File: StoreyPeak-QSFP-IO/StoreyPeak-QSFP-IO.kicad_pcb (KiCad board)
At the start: 2 copper layers, 30.1 x 69.8 mm, 29 parts, among them U1 QSFP_PCB-QSFP, U3 CH340G, X1 X322512MSB4SI

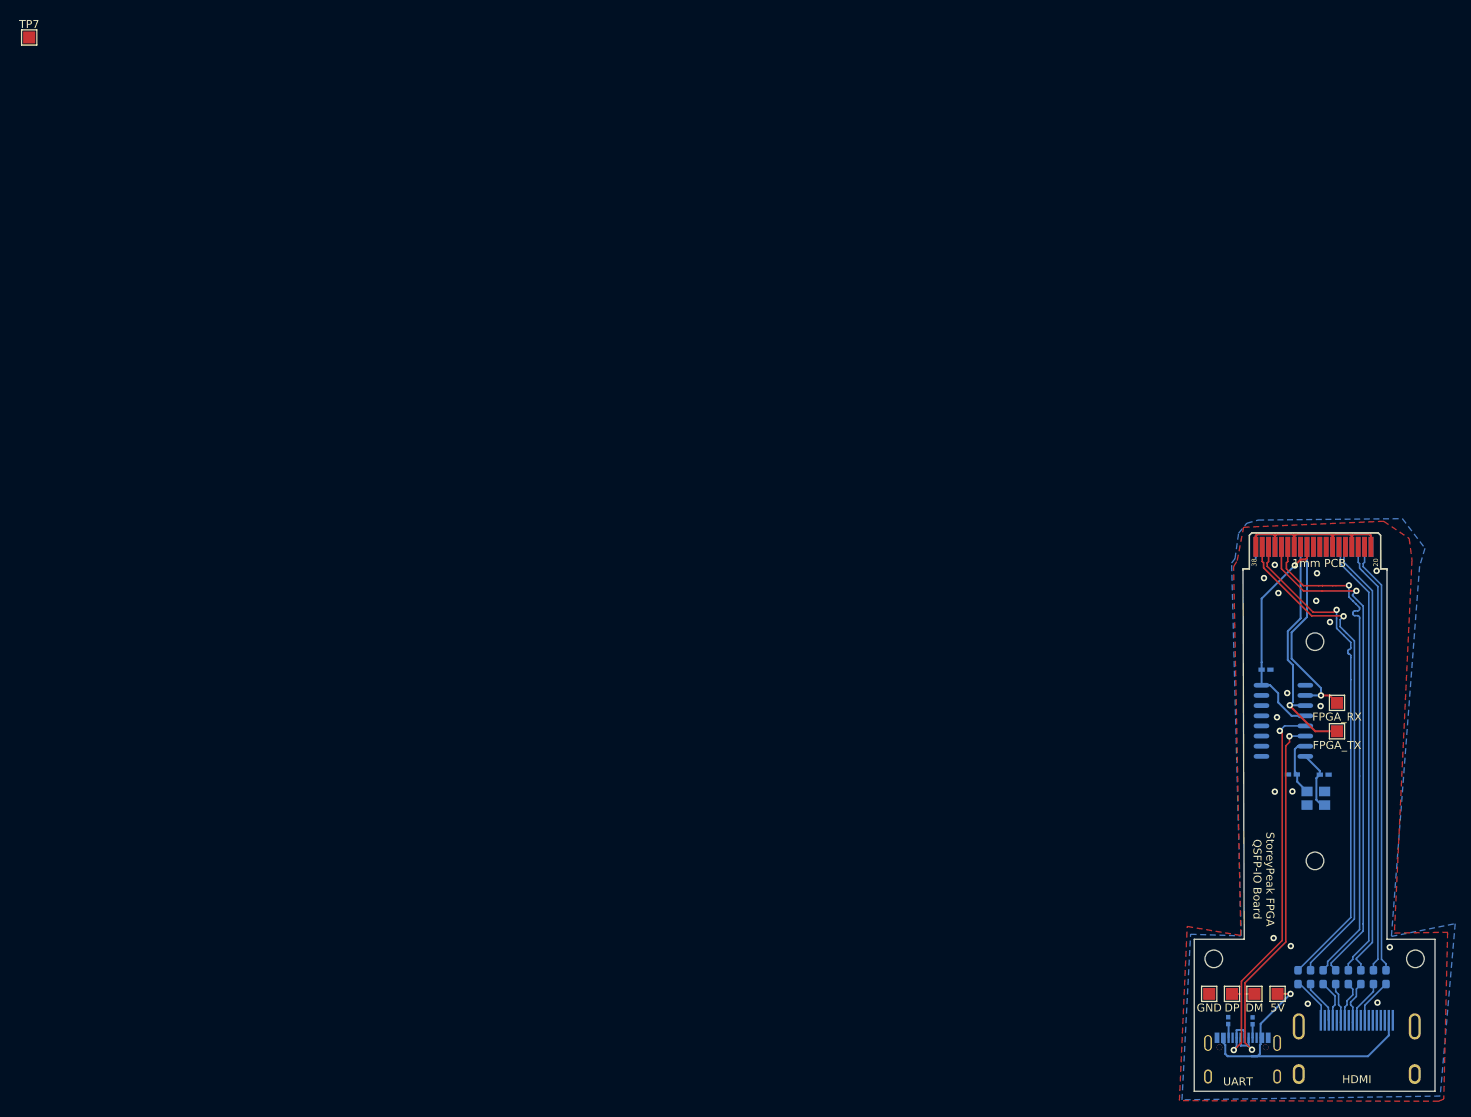
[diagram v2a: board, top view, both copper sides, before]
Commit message: Re-add accidentally deleted UART GND pad, move some traces to avoid cutting ground planes
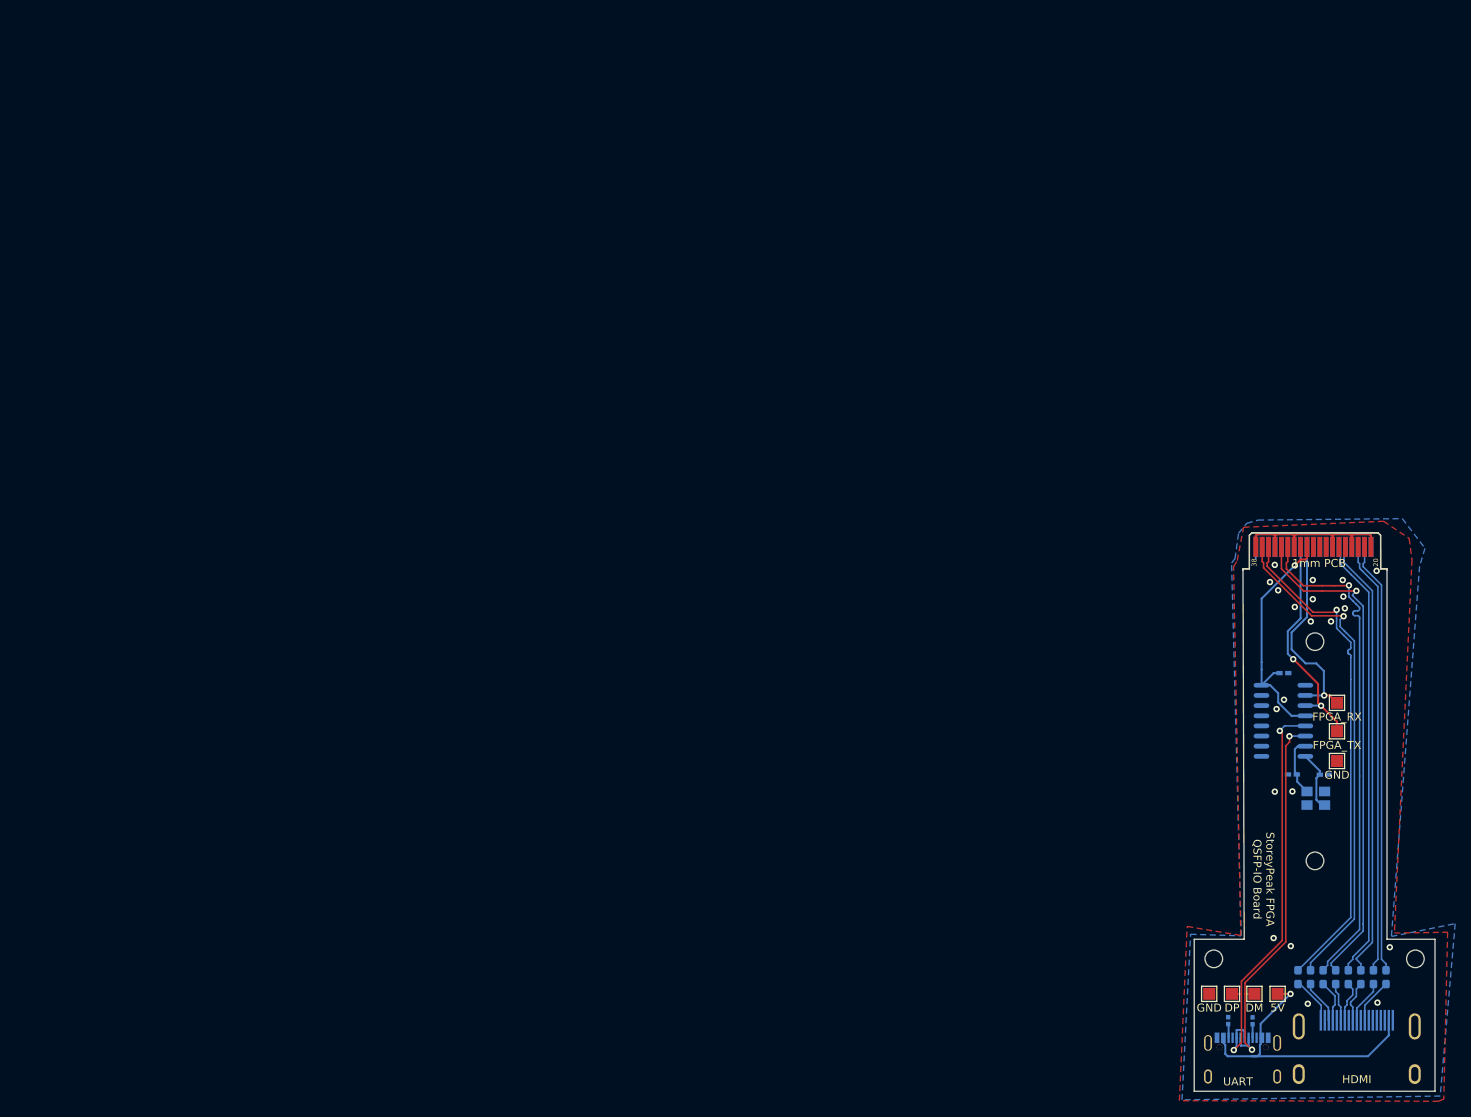
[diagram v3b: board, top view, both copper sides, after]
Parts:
- moved TP7 186.8 mm to (164.8, 91.7)
- moved C11 2.28 mm to (158.1, 80.7)
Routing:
- net +3V3: track 28.4 -> 31.3 mm
- net FPGA_TX: track 30.4 -> 28.3 mm, vias 1 -> 2
- net FPGA_RX: track 25.3 -> 26.1 mm
- net GND: vias 17 -> 21
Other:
- board text added: "GND"
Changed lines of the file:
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@@
 	(footprint "TestPoint:TestPoint_Pad_1.5x1.5mm"
 		(layer "F.Cu")
-		(at 1.275 1.275)
+		(at 164.75 91.72)
 		(descr "SMD rectangular pad as test Point, square 1.5mm side length")
 		(tags "test point SMD pad rectangle square")
@@
 			(at 0 -1.648 0)
 			(layer "F.SilkS")
+			(hide yes)
 			(effects
 				(font
@@
 	(footprint "easyeda2kicad:C0402"
 		(layer "B.Cu")
-		(at 155.875 80.3 180)
+		(at 158.11 80.73 180)
 		(property "Reference" "C11"
 			(at 0 4 180)
@@
 		)
 	)
+	(gr_text "GND"
+		(at 164.75 93.47 0)
+		(layer "F.SilkS")
+		(effects
+			(font
+				(size 1 1)
+				(thickness 0.15)
+			)
+		)
+	)
 	(gr_text "StoreyPeak FPGA\nQSFP-IO Board"
 		(at 155.575 106.5 -90)
@@
 	)
 	(via
-		(at 157.25 86.25)
+		(at 161.477438 74.272868)
+		(size 0.8)
+		(drill 0.4)
+		(layers "F.Cu" "B.Cu")
+		(free yes)
+		(net 1)
+	)
+	(via
+		(at 157.197195 85.222806)
 		(size 0.8)
 		(drill 0.4)
@@
 	)
 	(via
-		(at 162.7 84.85)
+		(at 161.725 71.49)
 		(size 0.8)
 		(drill 0.4)
@@
 	)
 	(via
-		(at 157.425 70.725)
+		(at 157.396078 70.379228)
 		(size 0.8)
 		(drill 0.4)
@@
 	)
 	(via
-		(at 162.25 68.25)
+		(at 161.725 69.1)
 		(size 0.8)
 		(drill 0.4)
@@
 	)
 	(via
-		(at 155.625 68.85)
+		(at 156.370772 69.353922)
 		(size 0.8)
 		(drill 0.4)
@@
 	)
 	(via
-		(at 169.81 121.92)
+		(at 165.543199 71.163998)
 		(size 0.8)
 		(drill 0.4)
@@
 	)
 	(via
-		(at 163.875 74.35)
+		(at 169.81 121.92)
 		(size 0.8)
 		(drill 0.4)
@@
 	)
 	(via
-		(at 162.15 71.7)
+		(at 164 74.273999)
 		(size 0.8)
 		(drill 0.4)
@@
 	)
 	(via
+		(at 159.475 72.463028)
+		(size 0.8)
+		(drill 0.4)
+		(layers "F.Cu" "B.Cu")
+		(free yes)
+		(net 1)
+	)
+	(via
+		(at 165.733589 72.637653)
+		(size 0.8)
+		(drill 0.4)
+		(layers "F.Cu" "B.Cu")
+		(free yes)
+		(net 1)
+	)
+	(via
 		(at 161.1 122.06)
 		(size 0.8)
@@
 	)
 	(via
-		(at 158.525 83.225)
+		(at 158.125 84.0625)
 		(size 0.8)
 		(drill 0.4)
@@
 	)
 	(via
+		(at 165.466629 69.1)
+		(size 0.8)
+		(drill 0.4)
+		(layers "F.Cu" "B.Cu")
+		(free yes)
+		(net 1)
+	)
+	(via
 		(at 156.975 67.2)
 		(size 0.8)
@@
 	)
 	(segment
-		(start 162.75 83.5)
-		(end 162.75 83.525)
+		(start 163.15 83.525)
+		(end 163.825 83.525)
 		(width 0.25)
 		(layer "F.Cu")
@@
 	)
 	(segment
-		(start 162.775 83.525)
-		(end 162.75 83.5)
+		(start 163.825 83.525)
+		(end 164.75 84.45)
 		(width 0.25)
 		(layer "F.Cu")
 		(net 21)
 	)
-	(segment
-		(start 162.75 83.525)
-		(end 162.775 83.525)
-		(width 0.25)
-		(layer "F.Cu")
+	(via
+		(at 163.15 83.525)
+		(size 0.8)
+		(drill 0.4)
+		(layers "F.Cu" "B.Cu")
 		(net 21)
 	)
 	(segment
-		(start 163.825 83.525)
-		(end 164.75 84.45)
+		(start 159.075 75.65)
+		(end 161 73.725)
 		(width 0.25)
-		(layer "F.Cu")
+		(layer "B.Cu")
 		(net 21)
 	)
 	(segment
-		(start 162.75 83.525)
-		(end 163.825 83.525)
+		(start 160.83 79.52)
+		(end 159.075 77.765)
 		(width 0.25)
-		(layer "F.Cu")
+		(layer "B.Cu")
 		(net 21)
 	)
-	(via
-		(at 162.75 83.525)
-		(size 0.8)
-		(drill 0.4)
-		(layers "F.Cu" "B.Cu")
+	(segment
+		(start 162.16 79.52)
+		(end 160.83 79.52)
+		(width 0.25)
+		(layer "B.Cu")
 		(net 21)
 	)
 	(segment
-		(start 159.075 78.925)
-		(end 162.75 82.6)
+		(start 163.15 83.525)
+		(end 160.795 83.525)
 		(width 0.25)
 		(layer "B.Cu")
@@
 	)
 	(segment
-		(start 159.075 75.65)
-		(end 159.075 78.925)
+		(start 163.11 83.485)
+		(end 163.11 80.47)
 		(width 0.25)
 		(layer "B.Cu")
@@
 	)
 	(segment
-		(start 161 73.725)
+		(start 159.075 77.765)
 		(end 159.075 75.65)
 		(width 0.25)
@@
 	)
 	(segment
-		(start 161 65)
-		(end 161 73.725)
+		(start 163.15 83.525)
+		(end 163.11 83.485)
 		(width 0.25)
 		(layer "B.Cu")
@@
 	)
 	(segment
-		(start 162.75 83.525)
-		(end 160.795 83.525)
+		(start 161 73.725)
+		(end 161 65)
 		(width 0.25)
 		(layer "B.Cu")
@@
 	)
 	(segment
-		(start 162.75 82.6)
-		(end 162.75 83.525)
+		(start 160.795 83.525)
+		(end 160.79 83.52)
 		(width 0.25)
 		(layer "B.Cu")
@@
 	)
 	(segment
-		(start 160.795 83.525)
-		(end 160.79 83.52)
+		(start 163.11 80.47)
+		(end 162.16 79.52)
 		(width 0.25)
 		(layer "B.Cu")
@@
 	)
 	(segment
-		(start 158.775 84.75)
-		(end 162.025 88)
+		(start 159.277347 78.992653)
+		(end 159.302653 78.992653)
+		(width 0.25)
+		(layer "F.Cu")
+		(net 27)
+	)
+	(segment
+		(start 164.75 86.8)
+		(end 162.76 84.81)
 		(width 0.25)
 		(layer "F.Cu")
@@
 	)
 	(segment
-		(start 158.775 84.675)
-		(end 158.775 84.75)
+		(start 164.75 88)
+		(end 164.75 86.8)
 		(width 0.25)
 		(layer "F.Cu")
@@
 	)
 	(segment
-		(start 158.7 84.75)
-		(end 158.7 84.75)
+		(start 162.39 82.08)
+		(end 162.39 84.44)
 		(width 0.25)
 		(layer "F.Cu")
@@
 	)
 	(segment
-		(start 162.025 88)
-		(end 164.75 88)
+		(start 162.39 84.44)
+		(end 162.76 84.81)
 		(width 0.25)
 		(layer "F.Cu")
@@
 	)
 	(segment
-		(start 158.775 84.75)
-		(end 158.7 84.75)
+		(start 159.302653 78.992653)
+		(end 162.39 82.08)
 		(width 0.25)
 		(layer "F.Cu")
@@
 	)
 	(via
-		(at 158.85 84.75)
+		(at 159.277347 78.992653)
 		(size 0.8)
 		(drill 0.4)
 		(layers "F.Cu" "B.Cu")
+		(free yes)
 		(net 27)
 	)
-	(segment
-		(start 160.75 84.75)
-		(end 160.79 84.79)
-		(width 0.25)
-		(layer "B.Cu")
+	(via
+		(at 162.76 84.81)
+		(size 0.8)
+		(drill 0.4)
+		(layers "F.Cu" "B.Cu")
+		(free yes)
 		(net 27)
 	)
@@
 	)
 	(segment
-		(start 159.25 79.736396)
-		(end 158.6 79.086396)
+		(start 160.75 84.75)
+		(end 160.79 84.79)
 		(width 0.25)
 		(layer "B.Cu")
@@
 	)
 	(segment
-		(start 158.6 79.086396)
-		(end 158.6 75.488604)
+		(start 162.74 84.79)
+		(end 162.76 84.81)
 		(width 0.25)
 		(layer "B.Cu")
@@
 	)
 	(segment
-		(start 158.85 84.75)
-		(end 160.75 84.75)
+		(start 159.277347 78.992653)
+		(end 158.6 78.315306)
 		(width 0.25)
 		(layer "B.Cu")
@@
 	)
 	(segment
-		(start 158.775 84.75)
-		(end 158.85 84.75)
+		(start 160.79 84.79)
+		(end 162.74 84.79)
 		(width 0.25)
 		(layer "B.Cu")
@@
 	)
 	(segment
-		(start 158.85 84.75)
-		(end 159.25 84.35)
-		(width 0.25)
-		(layer "B.Cu")
-		(net 27)
-	)
-	(segment
-		(start 159.25 84.35)
-		(end 159.25 79.736396)
+		(start 158.6 78.315306)
+		(end 158.6 75.488604)
 		(width 0.25)
 		(layer "B.Cu")
@@
 	)
 	(segment
+		(start 157.56 80.73)
+		(end 156.83 80.73)
+		(width 0.25)
+		(layer "B.Cu")
+		(net 42)
+	)
+	(segment
 		(start 157.4 84.400305)
 		(end 157.4 83.25)
@@
 		(width 0.25)
 		(layer "B.Cu")
+		(net 42)
+	)
+	(segment
+		(start 156.83 80.73)
+		(end 155.31 82.25)
+		(width 0.25)
+		(layer "B.Cu")

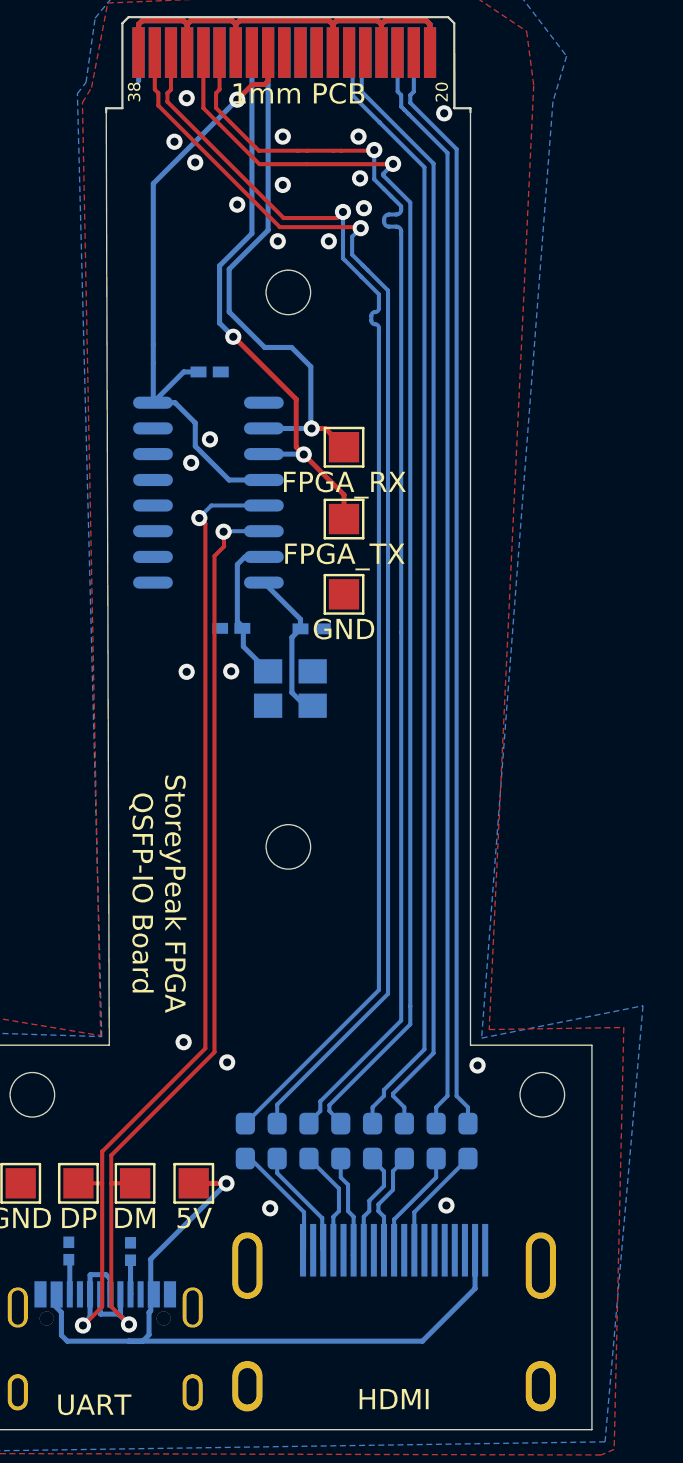
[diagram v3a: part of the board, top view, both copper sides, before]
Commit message: Add JLCPCB tooling holes
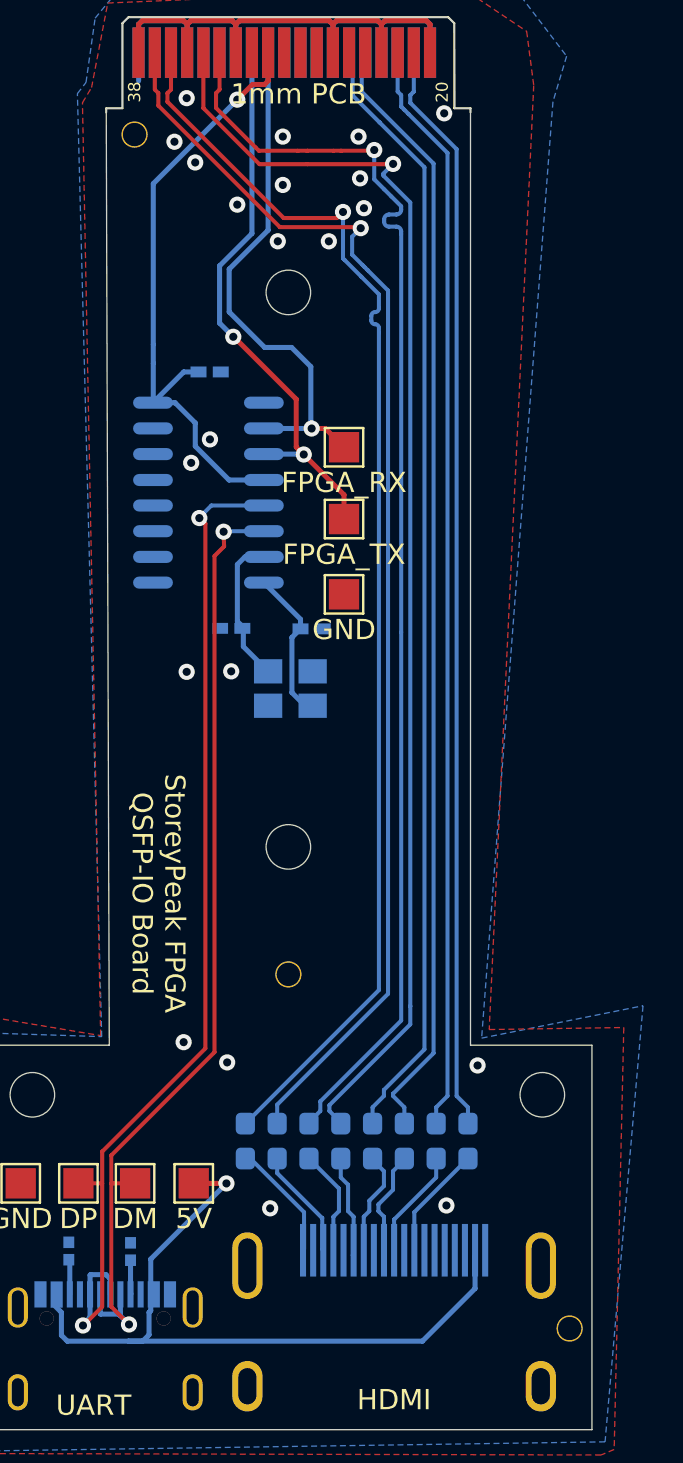
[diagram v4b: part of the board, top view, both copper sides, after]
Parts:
- added H5: JLC1, MountingHole:JLCPCB_Tooling_Hole, F.Cu at (154.4, 69.0)
- added H6: JLC2, MountingHole:JLCPCB_Tooling_Hole, F.Cu at (175.9, 128.0)
- added H7: JLC3, MountingHole:JLCPCB_Tooling_Hole, F.Cu at (162.0, 110.5)
